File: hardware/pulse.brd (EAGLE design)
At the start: 68.2 x 53.3 mm, 52 parts, among them IC1 MEGA8-P, IC2 MAX232, IC3 TL072P, IC4 7805, Q1 2N5485, Q2 16MHz

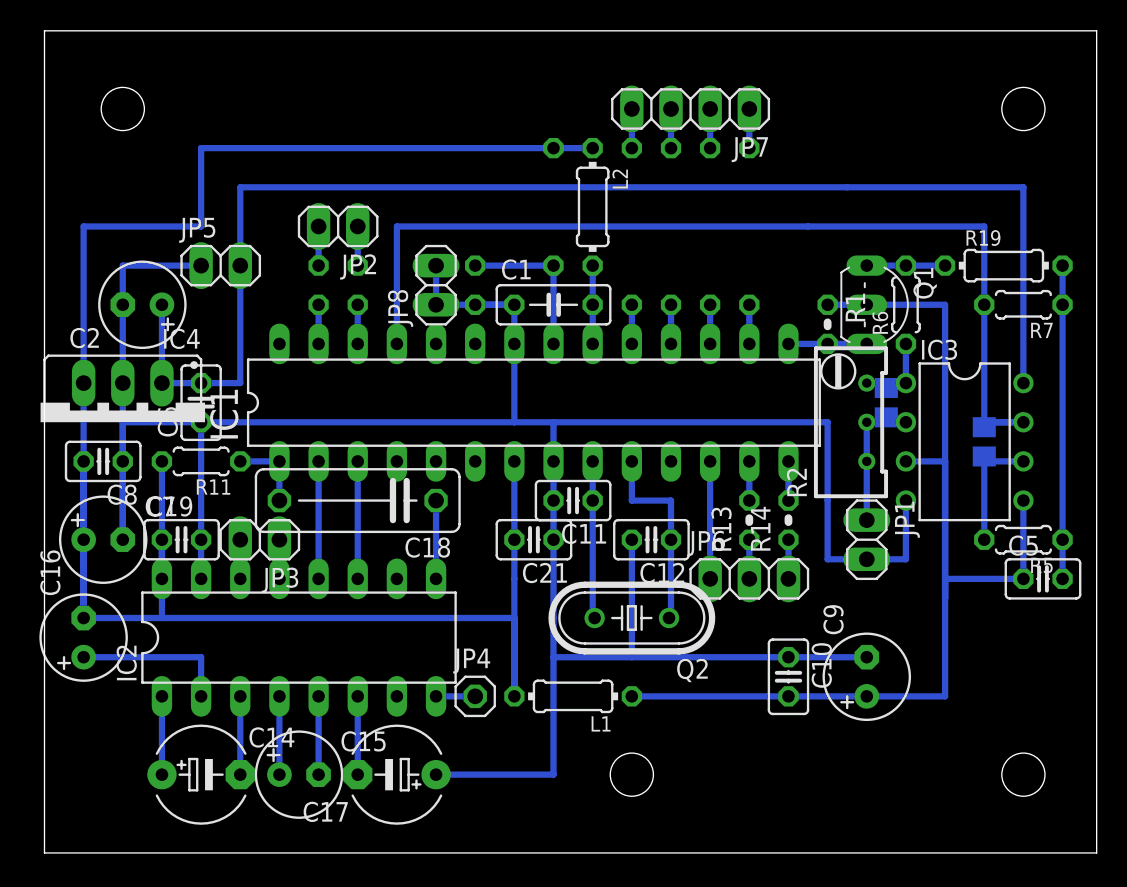
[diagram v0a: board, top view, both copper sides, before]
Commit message: Rewritten to large parts.
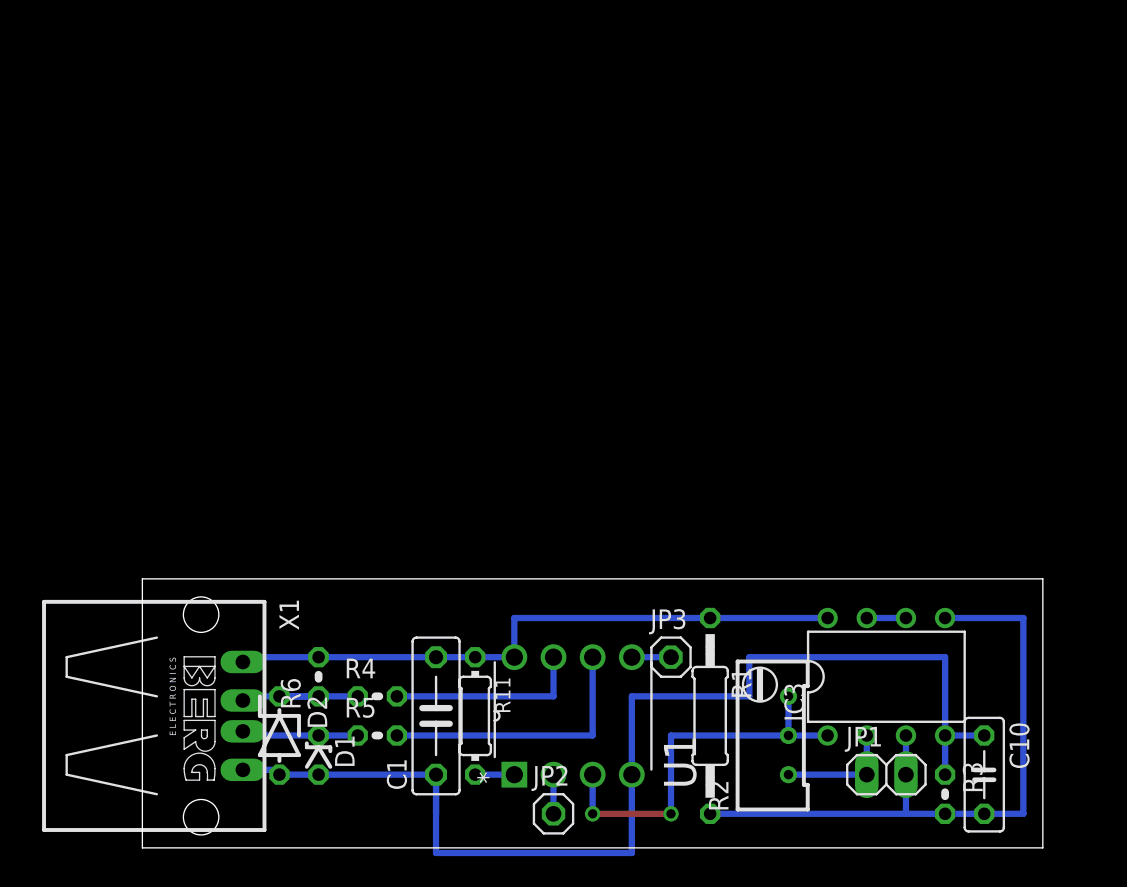
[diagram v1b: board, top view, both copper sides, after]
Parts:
- removed C11, C12: 22pF, rcl:C025-025X050
- removed C13, C19, C21, C5, C6, C8: 100nF, rcl:C025-025X050
- removed C14, C17: 1uF, rcl:E5-6
- removed C15, C16: 1uF, rcl:E2,5-6
- removed C18: 100nF, rcl:C102-043X133
- removed C2, C9: 100uF, rcl:E2,5-6
- removed C20: 68pF, rcl:C0805
- removed C4: 100nF, rcl:C0805
- removed C7: 10uF, rcl:E2,5-6
- removed IC1: MEGA8-P, atmel:DIL28-3
- removed IC2: MAX232, maxim:DIL16
- removed IC4: 7805, v-reg:78XXS
- removed JP4: DTR, pinhead:1X01
- removed JP5: Supply, pinhead:1X02
- removed JP6: LED1, pinhead:1X03
- removed JP7: LED2, pinhead:1X04
- removed JP8: GND, pinhead:1X02
- removed L1, L2: 100uH, rcl:0204/7
- removed Q1: 2N5485, transistor-fet:TO92-
- removed Q2: 16MHz, crystal:HC49/S
- removed R10: 10k, rcl:0204/7
- removed R13, R14: 1k5, rcl:0204V
- removed R15, R16, R17, R18: 1k5, rcl:0207/10
- removed R19: 500, rcl:0204/7
- removed R7: 1k5, rcl:0204/5
- removed R8, R9: 470, rcl:0204V
- added D1: 3.6V, diode:ZDIO-2.5
- added D2: 3.6V, diode:ZDIO-5
- added R3: 10k, rcl:0204V
- added R4: 68, rcl:0204V
- added U1: ATTINY45-20PU, Atmel_By_element14_Batch_1-00:DIP254P762X533-8
- added X1: (no value), con-berg:PN87520
- C1: device rcl:C050-025X075 -> rcl:C075-032X103
- C10: device rcl:C025-025X050 -> rcl:C050-025X075
- IC3: value TL072P -> TLC272P
- JP2: value LED -> (none); device pinhead:1X02 -> pinhead:1X01
- JP3: value Tx/RX -> (none); device pinhead:1X02 -> pinhead:1X01
- R1: value 1M -> 10k; device rcl:0204V -> rcl:0207/12
- R11: device rcl:0204/5 -> rcl:0204/7
- R5: value 1k5 -> 68; device rcl:0204/5 -> rcl:0204V
- R6: value 1k -> 2.2k; device rcl:0204/5 -> rcl:0204V
- moved R6 45.1 mm to (17.8, 11.4)
- moved R5 43.8 mm to (21.6, 7.62), turned to 0 degrees
- moved JP2 40.6 mm to (33.0, 2.54), turned to 0 degrees
- moved C1 27.7 mm to (25.4, 8.89), turned to 90 degrees
- moved JP3 27.7 mm to (40.6, 12.7), turned to 0 degrees
- moved R1 26.5 mm to (43.2, 8.89)
- moved R11 24.3 mm to (27.9, 8.89), turned to 270 degrees
- moved R2 20.9 mm to (47.0, 7.62)
- moved IC3 16.1 mm to (54.6, 11.4), turned to 0 degrees
- moved JP1 15.3 mm to (54.6, 5.08), turned to 0 degrees
- moved C10 14.2 mm to (61.0, 5.08)
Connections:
- removed net N$13: JP2.2, R8.1
- removed net N$14: JP2.1, R9.1
- removed net N$15: C11.1, IC1.9, Q2.2
- removed net N$16: C12.1, IC1.10, Q2.1
- removed net N$17: C16.+, IC2.2
- removed net N$18: C17.-, IC2.6
- removed net N$19: C13.2, IC1.21, R10.1
- removed net N$2: C20.2, IC3.1, R2.3, R6.1
- removed net N$20: IC2.14, JP3.2
- removed net N$21: IC2.13, JP3.1
- removed net N$22: IC2.8, JP4.1
- removed net N$23: C14.-, IC2.3
- removed net N$24: C14.+, IC2.1
- removed net N$25: C15.+, IC2.4
- removed net N$26: C15.-, IC2.5
- removed net N$27: C18.2, IC1.1, R11.1
- removed net N$28: C18.1, IC2.9
- removed net N$29: IC1.3, IC2.11
- removed net N$30: IC1.2, IC2.12
- removed net N$31: IC1.15, Q1.1, R1.2
- removed net N$32: IC1.27, R8.2
- removed net N$33: IC1.26, R9.2
- removed net N$34: JP6.3, R14.1
- removed net N$35: JP6.2, R13.1
- removed net N$38: JP7.1, R15.1
- removed net N$39: JP7.2, R16.1
- removed net N$40: JP7.3, R18.1
- removed net N$41: JP7.4, R17.1
- removed net N$45: IC1.13, R13.2
- removed net N$46: IC1.14, R14.2
- removed net N$47: IC1.16, R15.2
- removed net N$48: IC1.17, R16.2
- removed net N$49: IC1.18, R18.2
- removed net N$50: IC1.19, R17.2
- removed net VCC: C2.+, C6.2, IC3.8, IC4.IN, JP5.2
- new net N$10: D1.C, R5.1, X1.3
- new net N$5: JP3.1, U1.5
- new net N$9: R11.2, U1.1
- net +5V: now also C1.2, IC3.8, R1.1, R11.1, R6.2, U1.8, X1.1; no longer C16.-, C19.1, C21.2, C7.+, C8.2, IC1.7, IC2.16, IC4.OUT, L1.2, L2.1, R10.2, R11.2
- net GND: now also D1.A, D2.A, R3.1, U1.4, X1.4; no longer C11.2, C12.2, C13.1, C17.+, C19.2, C2.-, C21.1, C6.1, C7.-, C8.1, C9.-, IC1.22, IC1.8, IC2.15, IC4.GND, JP1.2, JP5.1, JP8.1, JP8.2
- net N$1: no longer C20.1, R2.2
- net N$11: now also D2.C, R4.1, R6.1, X1.2; no longer IC1.12, JP6.1
- net N$3: now also R4.2, U1.7; no longer Q1.3, R19.1, R6.2
- net N$4: now also JP2.1, U1.2; no longer C1.2, IC1.20, L2.2
- net N$6: now also U1.6; no longer C4.2, IC3.6
- net N$7: now also IC3.6, IC3.7; no longer C5.2, R19.2, R5.1, R7.1
- net N$8: now also IC3.1, R2.2, R2.3, U1.3; no longer C4.1, IC1.25, IC3.7, R7.2
- net VCC/2: now also JP1.2, R1.2, R3.2; no longer C5.1, C9.+, L1.1, Q1.2, R1.1
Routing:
- net GND: track 180.3 -> 76.3 mm
- net +5V: track 142.2 -> 40.8 mm
- net VCC: track 86.4 -> 0.00 mm
- net N$8: track 64.1 -> 25.4 mm, vias 0 -> 2
- net VCC/2: track 76.2 -> 43.2 mm
- net N$7: track 20.3 -> 2.54 mm
- net N$16: track 12.8 -> 0.00 mm
- net N$15: track 10.3 -> 0.00 mm
- net N$19: track 10.2 -> 0.00 mm
- net N$17: track 10.2 -> 0.00 mm
- net N$6: track 8.26 -> 17.8 mm
- net N$10: track 0.00 -> 7.72 mm
- net N$3: track 5.08 -> 12.7 mm
- net N$30: track 7.62 -> 0.00 mm
- net N$29: track 7.62 -> 0.00 mm
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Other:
- board size 68.2 x 53.3 mm -> 58.4 x 17.5 mm
- board text removed: "Pulse rev. 1"
- board text removed: "fits into TEKO 2/A"

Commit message: Fixed minors.
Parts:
- JP2: value (none) -> LED2
- JP3: value (none) -> LED1
- moved R5 1.27 mm to (21.6, 8.89)
- moved R4 1.27 mm to (21.6, 8.89), turned to 270 degrees
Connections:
- removed net N$6: R5.2, U1.6
- new net N$2: R5.2, U1.7
- net N$3: now also U1.6; no longer U1.7
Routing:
- net N$6: track 17.8 -> 0.00 mm
- net N$2: track 0.00 -> 14.0 mm
- net N$3: track 12.7 -> 19.1 mm
- net N$11: track 10.3 -> 11.5 mm
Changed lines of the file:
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@@
 <element name="R11" library="rcl" package="0204/7" value="10k" x="27.94" y="8.89" rot="R270"/>
 <element name="JP1" library="pinhead" package="1X02" value="IN" x="54.61" y="5.08"/>
-<element name="U1" library="Atmel_By_element14_Batch_1-00" package="DIP254P762X533-8" value="ATTINY45-20PU" x="38.1" y="12.7" rot="R90">
+<element name="U1" library="Atmel_By_element14_Batch_1-00" package="DIP254P762X533-8" value="ATTINY45-20PU" x="38.1" y="12.7" smashed="yes" rot="R90">
 <attribute name="OC_FARNELL" value="1288352" x="38.1" y="12.7" size="1.778" layer="27" rot="R90" display="off"/>
 <attribute name="MPN" value="ATTINY45-20PU" x="38.1" y="12.7" size="1.778" layer="27" rot="R90" display="off"/>
@@
 <attribute name="OC_NEWARK" value="23M5072" x="38.1" y="12.7" size="1.778" layer="27" rot="R90" display="off"/>
 <attribute name="SUPPLIER" value="Atmel" x="38.1" y="12.7" size="1.778" layer="27" rot="R90" display="off"/>
+<attribute name="NAME" x="42.2656" y="4.1402" size="2.0828" layer="25" ratio="10" rot="SR90"/>
+<attribute name="VALUE" x="18.1356" y="14.605" size="2.0828" layer="27" ratio="10" rot="SR0"/>
 </element>
 <element name="R1" library="rcl" package="0207/12" value="10k" x="43.18" y="8.89" rot="R270"/>
@@
 <attribute name="MF" value="" x="10.16" y="8.89" size="1.778" layer="27" rot="R270" display="off"/>
 </element>
-<element name="R4" library="rcl" package="0204V" value="68" x="21.59" y="10.16"/>
-<element name="R5" library="rcl" package="0204V" value="68" x="21.59" y="7.62"/>
+<element name="R4" library="rcl" package="0204V" value="68" x="21.59" y="8.89" rot="R270"/>
+<element name="R5" library="rcl" package="0204V" value="68" x="21.59" y="8.89"/>
 <element name="D1" library="diode" package="ZDIO-2.5" value="3.6V" x="17.78" y="6.35" rot="R270"/>
 <element name="D2" library="diode" package="ZDIO-5" value="3.6V" x="15.24" y="7.62" rot="R270"/>
 <element name="R6" library="rcl" package="0204V" value="2.2k" x="17.78" y="11.43" rot="R90"/>
 <element name="C1" library="rcl" package="C075-032X103" value="100nF" x="25.4" y="8.89" rot="R90"/>
-<element name="JP2" library="pinhead" package="1X01" value="" x="33.02" y="2.54"/>
-<element name="JP3" library="pinhead" package="1X01" value="" x="40.64" y="12.7"/>
+<element name="JP2" library="pinhead" package="1X01" value="LED2" x="33.02" y="2.54"/>
+<element name="JP3" library="pinhead" package="1X01" value="LED1" x="40.64" y="12.7"/>
 <element name="R2" library="rcl" package="RTRIM64W" value="10k" x="46.99" y="7.62"/>
 </elements>
@@
 <contactref element="D1" pad="C"/>
 <contactref element="X1" pad="3"/>
-<wire x1="20.32" y1="7.62" x2="17.78" y2="7.62" width="0.4064" layer="16"/>
+<wire x1="20.32" y1="8.89" x2="17.78" y2="7.62" width="0.4064" layer="16"/>
 <wire x1="17.78" y1="7.62" x2="12.87" y2="7.62" width="0.4064" layer="16"/>
 <wire x1="12.87" y1="7.62" x2="12.87" y2="7.89" width="0.4064" layer="16"/>
@@
 <contactref element="R6" pad="1"/>
 <wire x1="17.78" y1="10.16" x2="15.24" y2="10.16" width="0.4064" layer="16"/>
-<wire x1="20.32" y1="10.16" x2="15.24" y2="10.16" width="0.4064" layer="16"/>
+<wire x1="21.59" y1="10.16" x2="15.24" y2="10.16" width="0.4064" layer="16"/>
 <wire x1="15.24" y1="10.16" x2="12.87" y2="10.16" width="0.4064" layer="16"/>
 <wire x1="12.87" y1="10.16" x2="12.87" y2="9.89" width="0.4064" layer="16"/>
-</signal>
-<signal name="N$3">
-<contactref element="R4" pad="2"/>
-<contactref element="U1" pad="7"/>
-<wire x1="33.02" y1="12.7" x2="33.02" y2="10.16" width="0.4064" layer="16"/>
-<wire x1="33.02" y1="10.16" x2="22.86" y2="10.16" width="0.4064" layer="16"/>
-</signal>
-<signal name="N$6">
-<contactref element="R5" pad="2"/>
-<contactref element="U1" pad="6"/>
-<wire x1="35.56" y1="12.7" x2="35.56" y2="7.62" width="0.4064" layer="16"/>
-<wire x1="35.56" y1="7.62" x2="22.86" y2="7.62" width="0.4064" layer="16"/>
 </signal>
 <signal name="N$8">
@@
 <wire x1="38.1" y1="12.7" x2="40.64" y2="12.7" width="0.4064" layer="16"/>
 </signal>
+<signal name="N$2">
+<contactref element="U1" pad="7"/>
+<contactref element="R5" pad="2"/>
+<wire x1="22.86" y1="8.89" x2="22.86" y2="10.16" width="0.4064" layer="16"/>
+<wire x1="22.86" y1="10.16" x2="33.02" y2="10.16" width="0.4064" layer="16"/>
+<wire x1="33.02" y1="10.16" x2="33.02" y2="12.7" width="0.4064" layer="16"/>
+</signal>
+<signal name="N$3">
+<contactref element="R4" pad="2"/>
+<contactref element="U1" pad="6"/>
+<wire x1="21.59" y1="7.62" x2="35.56" y2="7.62" width="0.4064" layer="16"/>
+<wire x1="35.56" y1="7.62" x2="35.56" y2="12.7" width="0.4064" layer="16"/>
+</signal>
 </signals>

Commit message: Updated schematic & board.
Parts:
- removed X1: (no value), con-berg:PN87520
- added X2: USB-A, adafruit:MOLEX_480371000
- R2: value 10k -> 500k
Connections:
- net +5V: now also X2.1; no longer X1.1
- net GND: now also X2.4; no longer X1.4
- net N$10: now also X2.3; no longer X1.3
- net N$11: now also X2.2; no longer X1.2
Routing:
- net +5V: track 40.8 -> 42.3 mm
- net N$11: track 11.5 -> 12.9 mm
- net N$10: track 8.02 -> 9.40 mm
- net GND: track 76.3 -> 77.7 mm
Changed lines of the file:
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@@
 <element name="R1" library="rcl" package="0207/12" value="10k" x="43.18" y="8.89" rot="R270"/>
 <element name="R3" library="rcl" package="0204V" value="10k" x="58.42" y="3.81" rot="R270"/>
-<element name="X1" library="con-berg" package="PN87520" value="" x="10.16" y="8.89" rot="R270">
-<attribute name="OC_FARNELL" value="unknown" x="10.16" y="8.89" size="1.778" layer="27" rot="R270" display="off"/>
-<attribute name="MPN" value="" x="10.16" y="8.89" size="1.778" layer="27" rot="R270" display="off"/>
-<attribute name="OC_NEWARK" value="unknown" x="10.16" y="8.89" size="1.778" layer="27" rot="R270" display="off"/>
-<attribute name="MF" value="" x="10.16" y="8.89" size="1.778" layer="27" rot="R270" display="off"/>
-</element>
 <element name="R4" library="rcl" package="0204V" value="68" x="21.59" y="8.89" rot="R270"/>
 <element name="R5" library="rcl" package="0204V" value="68" x="21.59" y="8.89"/>
@@
 <element name="JP2" library="pinhead" package="1X01" value="LED2" x="33.02" y="2.54"/>
 <element name="JP3" library="pinhead" package="1X01" value="LED1" x="40.64" y="12.7"/>
-<element name="R2" library="rcl" package="RTRIM64W" value="10k" x="46.99" y="7.62"/>
+<element name="R2" library="rcl" package="RTRIM64W" value="500k" x="46.99" y="7.62"/>
+<element name="X2" library="adafruit" package="MOLEX_480371000" value="USB-A" x="8.89" y="8.89" rot="MR90"/>
 </elements>
 <signals>
@@
 <contactref element="IC3" pad="4"/>
 <contactref element="U1" pad="4"/>
-<contactref element="X1" pad="4"/>
 <contactref element="D1" pad="A"/>
 <contactref element="D2" pad="A"/>
-<wire x1="15.24" y1="5.08" x2="15.24" y2="5.39" width="0.4064" layer="16"/>
-<wire x1="15.24" y1="5.39" x2="12.87" y2="5.39" width="0.4064" layer="16"/>
 <contactref element="R3" pad="1"/>
 <wire x1="15.24" y1="5.08" x2="17.78" y2="5.08" width="0.4064" layer="16"/>
@@
 <wire x1="58.42" y1="12.7" x2="58.42" y2="7.62" width="0.4064" layer="16"/>
 <wire x1="60.96" y1="7.62" x2="58.42" y2="7.62" width="0.4064" layer="16"/>
+<contactref element="X2" pad="4"/>
+<wire x1="15.24" y1="5.08" x2="11.49" y2="5.08" width="0.4064" layer="16"/>
+<wire x1="11.49" y1="5.08" x2="11.49" y2="5.39" width="0.4064" layer="16"/>
 </signal>
 <signal name="N$1">
@@
 <contactref element="U1" pad="8"/>
 <contactref element="IC3" pad="8"/>
-<contactref element="X1" pad="1"/>
 <contactref element="R6" pad="2"/>
 <contactref element="R1" pad="1"/>
-<wire x1="12.87" y1="12.39" x2="12.87" y2="12.7" width="0.4064" layer="16"/>
 <wire x1="27.94" y1="12.7" x2="25.4" y2="12.7" width="0.4064" layer="16"/>
 <wire x1="25.4" y1="12.7" x2="17.78" y2="12.7" width="0.4064" layer="16"/>
@@
 <wire x1="30.48" y1="15.24" x2="43.18" y2="15.24" width="0.4064" layer="16"/>
 <contactref element="C1" pad="2"/>
-<wire x1="12.87" y1="12.7" x2="17.78" y2="12.7" width="0.4064" layer="16"/>
+<wire x1="11.43" y1="12.7" x2="17.78" y2="12.7" width="0.4064" layer="16"/>
 <wire x1="27.94" y1="12.7" x2="30.48" y2="12.7" width="0.4064" layer="16"/>
 <wire x1="43.18" y1="15.24" x2="50.8" y2="15.24" width="0.4064" layer="16"/>
+<contactref element="X2" pad="1"/>
+<wire x1="11.49" y1="12.39" x2="11.43" y2="12.39" width="0.4064" layer="16"/>
+<wire x1="11.43" y1="12.39" x2="11.43" y2="12.7" width="0.4064" layer="16"/>
 </signal>
 <signal name="N$7">
@@
 <contactref element="R5" pad="1"/>
 <contactref element="D1" pad="C"/>
-<contactref element="X1" pad="3"/>
 <wire x1="20.32" y1="8.89" x2="17.78" y2="7.62" width="0.4064" layer="16"/>
-<wire x1="17.78" y1="7.62" x2="12.87" y2="7.62" width="0.4064" layer="16"/>
-<wire x1="12.87" y1="7.62" x2="12.87" y2="7.89" width="0.4064" layer="16"/>
+<wire x1="17.78" y1="7.62" x2="11.49" y2="7.62" width="0.4064" layer="16"/>
+<contactref element="X2" pad="3"/>
+<wire x1="11.49" y1="7.62" x2="11.49" y2="7.89" width="0.4064" layer="16"/>
 </signal>
 <signal name="N$11">
 <contactref element="R4" pad="1"/>
 <contactref element="D2" pad="C"/>
-<contactref element="X1" pad="2"/>
 <contactref element="R6" pad="1"/>
 <wire x1="17.78" y1="10.16" x2="15.24" y2="10.16" width="0.4064" layer="16"/>
 <wire x1="21.59" y1="10.16" x2="15.24" y2="10.16" width="0.4064" layer="16"/>
-<wire x1="15.24" y1="10.16" x2="12.87" y2="10.16" width="0.4064" layer="16"/>
-<wire x1="12.87" y1="10.16" x2="12.87" y2="9.89" width="0.4064" layer="16"/>
+<wire x1="15.24" y1="10.16" x2="11.49" y2="10.16" width="0.4064" layer="16"/>
+<contactref element="X2" pad="2"/>
+<wire x1="11.49" y1="10.16" x2="11.49" y2="9.89" width="0.4064" layer="16"/>
 </signal>
 <signal name="N$8">
